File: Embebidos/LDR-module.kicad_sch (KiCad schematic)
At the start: 10 parts, among them U2 LM358

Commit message: anotaciones_fix
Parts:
- renumbered R14 to R15, R15 to R16, R16 to R17, R17 to R18
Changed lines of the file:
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@@
   (symbol (lib_id "Device:R") (at 144.78 43.18 0) (unit 1)
     (in_bom yes) (on_board yes) (fields_autoplaced)
-    (property "Reference" "R17" (id 0) (at 147.32 41.9099 0)
+    (property "Reference" "R18" (id 0) (at 147.32 41.9099 0)
       (effects (font (size 1.27 1.27)) (justify left))
     )
@@
   (symbol (lib_id "power:GND") (at 55.88 67.31 0) (unit 1)
     (in_bom yes) (on_board yes) (fields_autoplaced)
-    (property "Reference" "#PWR018" (id 0) (at 55.88 73.66 0)
+    (property "Reference" "#PWR019" (id 0) (at 55.88 73.66 0)
       (effects (font (size 1.27 1.27)) hide)
     )
@@
   (symbol (lib_id "power:GND") (at 116.84 54.61 0) (unit 1)
     (in_bom yes) (on_board yes) (fields_autoplaced)
-    (property "Reference" "#PWR021" (id 0) (at 116.84 60.96 0)
+    (property "Reference" "#PWR022" (id 0) (at 116.84 60.96 0)
       (effects (font (size 1.27 1.27)) hide)
     )
@@
   (symbol (lib_id "Device:R") (at 68.58 54.61 0) (unit 1)
     (in_bom yes) (on_board yes) (fields_autoplaced)
-    (property "Reference" "R14" (id 0) (at 71.12 53.3399 0)
+    (property "Reference" "R15" (id 0) (at 71.12 53.3399 0)
       (effects (font (size 1.27 1.27)) (justify left))
     )
@@
   (symbol (lib_id "Sensor_Optical:LDR07") (at 96.52 67.31 0) (unit 1)
     (in_bom yes) (on_board yes) (fields_autoplaced)
-    (property "Reference" "R16" (id 0) (at 99.06 66.0399 0)
+    (property "Reference" "R17" (id 0) (at 99.06 66.0399 0)
       (effects (font (size 1.27 1.27)) (justify left))
     )
@@
   (symbol (lib_id "Device:R") (at 96.52 54.61 0) (unit 1)
     (in_bom yes) (on_board yes) (fields_autoplaced)
-    (property "Reference" "R15" (id 0) (at 99.06 53.3399 0)
+    (property "Reference" "R16" (id 0) (at 99.06 53.3399 0)
       (effects (font (size 1.27 1.27)) (justify left))
     )
@@
   (symbol (lib_id "power:+5V") (at 55.88 46.99 0) (unit 1)
     (in_bom yes) (on_board yes) (fields_autoplaced)
-    (property "Reference" "#PWR017" (id 0) (at 55.88 50.8 0)
+    (property "Reference" "#PWR018" (id 0) (at 55.88 50.8 0)
       (effects (font (size 1.27 1.27)) hide)
     )
@@
   (symbol (lib_id "power:GND") (at 90.17 77.47 0) (unit 1)
     (in_bom yes) (on_board yes) (fields_autoplaced)
-    (property "Reference" "#PWR020" (id 0) (at 90.17 83.82 0)
+    (property "Reference" "#PWR021" (id 0) (at 90.17 83.82 0)
       (effects (font (size 1.27 1.27)) hide)
     )
@@
   (symbol (lib_id "power:+5V") (at 90.17 35.56 0) (unit 1)
     (in_bom yes) (on_board yes) (fields_autoplaced)
-    (property "Reference" "#PWR019" (id 0) (at 90.17 39.37 0)
-      (effects (font (size 1.27 1.27)) hide)
-    )
+    (property "Reference" "#PWR020" (id 0) (at 90.17 39.37 0)
+      (effects (font (size 1.27 1.27)) hide)
+    )

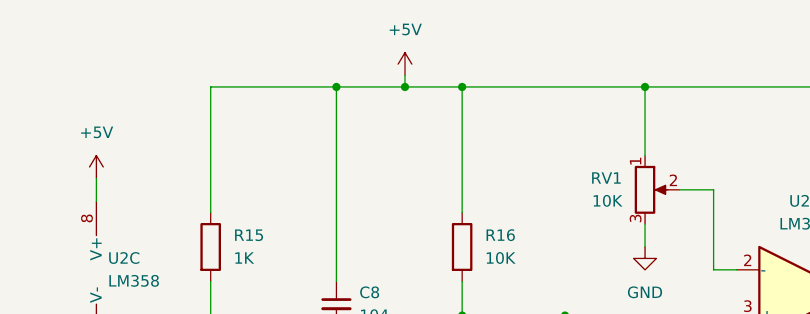
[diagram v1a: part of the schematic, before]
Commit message: cambio LDR
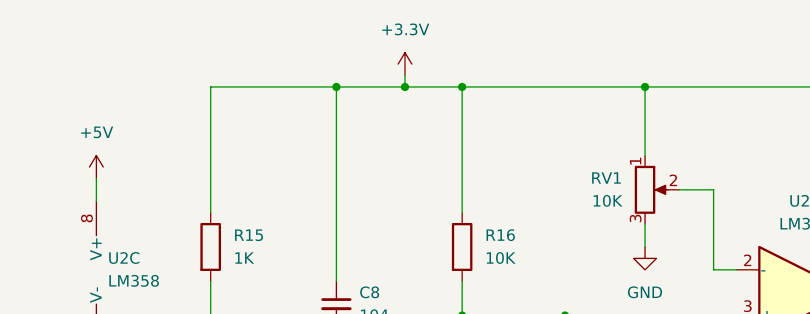
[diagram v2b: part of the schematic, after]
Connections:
- net +5V: no longer C8.1, R15.1, R16.1, R18.1, RV1.1
- new net +3.3V: C8.1, R15.1, R16.1, R18.1, RV1.1
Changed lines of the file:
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@@
     (pin "2")
+  )
+  (symbol (lib_id "power:+3.3V") (at 90.17 35.56 0) (unit 1)
+    (in_bom yes) (on_board yes) (fields_autoplaced)
+    (property "Reference" "#PWR?" (id 0) (at 90.17 39.37 0)
+      (effects (font (size 1.27 1.27)) hide)
+    )
+    (property "Value" "+3.3V" (id 1) (at 90.17 30.48 0))
+    (property "Footprint" "" (id 2) (at 90.17 35.56 0)
+      (effects (font (size 1.27 1.27)) hide)
+    )
+    (property "Datasheet" "" (id 3) (at 90.17 35.56 0)
+      (effects (font (size 1.27 1.27)) hide)
+    )
+    (pin "1")
   )
   (symbol (lib_id "power:GND") (at 55.88 67.31 0) (unit 1)
@@
       (effects (font (size 1.27 1.27)) hide)
     )
-    (pin "1")
-  )
-  (symbol (lib_id "power:+5V") (at 90.17 35.56 0) (unit 1)
-    (in_bom yes) (on_board yes) (fields_autoplaced)
-    (property "Reference" "#PWR020" (id 0) (at 90.17 39.37 0)
-      (effects (font (size 1.27 1.27)) hide)
-    )
-    (property "Value" "+5V" (id 1) (at 90.17 30.48 0))
-    (property "Footprint" "" (id 2) (at 90.17 35.56 0)
-      (effects (font (size 1.27 1.27)) hide)
-    )
-    (property "Datasheet" "" (id 3) (at 90.17 35.56 0)
-      (effects (font (size 1.27 1.27)) hide)
-    )

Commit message: wii
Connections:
- net +3.3V is gone; now on net +5V: C8.1, R15.1, R16.1, R18.1, RV1.1
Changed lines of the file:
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@@
     (pin "2")
-  )
-  (symbol (lib_id "power:+3.3V") (at 90.17 35.56 0) (unit 1)
-    (in_bom yes) (on_board yes) (fields_autoplaced)
-    (property "Reference" "#PWR?" (id 0) (at 90.17 39.37 0)
-      (effects (font (size 1.27 1.27)) hide)
-    )
-    (property "Value" "+3.3V" (id 1) (at 90.17 30.48 0))
-    (property "Footprint" "" (id 2) (at 90.17 35.56 0)
-      (effects (font (size 1.27 1.27)) hide)
-    )
-    (property "Datasheet" "" (id 3) (at 90.17 35.56 0)
-      (effects (font (size 1.27 1.27)) hide)
-    )
-    (pin "1")
   )
   (symbol (lib_id "power:GND") (at 55.88 67.31 0) (unit 1)
@@
       (effects (font (size 1.27 1.27)) hide)
     )
+    (pin "1")
+  )
+  (symbol (lib_id "power:+5V") (at 90.17 35.56 0) (unit 1)
+    (in_bom yes) (on_board yes) (fields_autoplaced)
+    (property "Reference" "#PWR020" (id 0) (at 90.17 39.37 0)
+      (effects (font (size 1.27 1.27)) hide)
+    )
+    (property "Value" "+5V" (id 1) (at 90.17 30.48 0))
+    (property "Footprint" "" (id 2) (at 90.17 35.56 0)
+      (effects (font (size 1.27 1.27)) hide)
+    )
+    (property "Datasheet" "" (id 3) (at 90.17 35.56 0)
+      (effects (font (size 1.27 1.27)) hide)
+    )

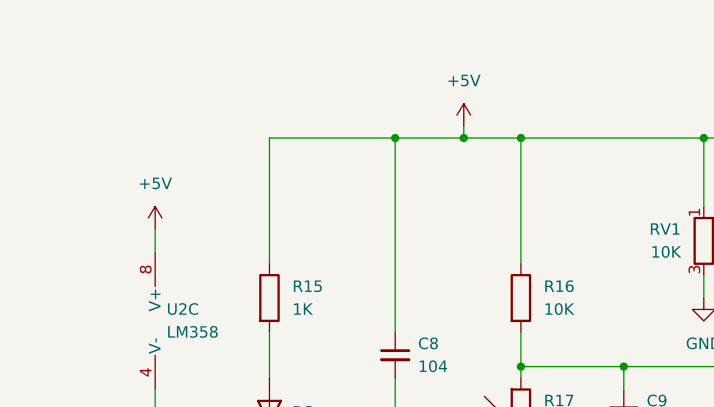
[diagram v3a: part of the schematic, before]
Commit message: Cambio de anotacion y Vcc ldr
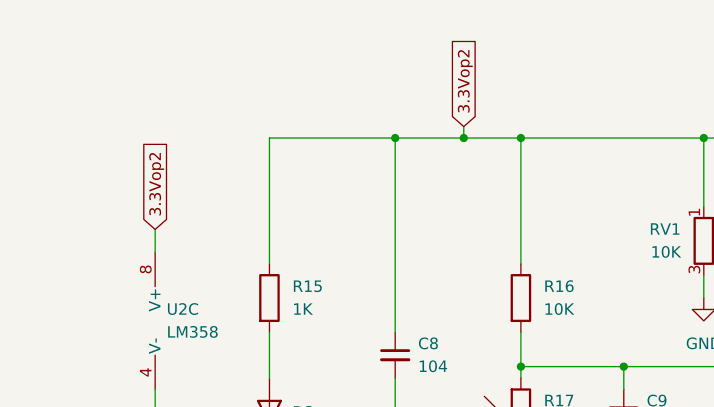
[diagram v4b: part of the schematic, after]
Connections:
- net +5V renamed 3.3Vop2
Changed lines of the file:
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@@
     (effects (font (size 1.27 1.27)) (justify left bottom))
+  )
+  (global_label "3.3Vop2" (shape input) (at 55.88 46.99 90) (fields_autoplaced)
+    (effects (font (size 1.27 1.27)) (justify left))
+    (property "Intersheet References" "${INTERSHEET_REFS}" (id 0) (at 55.8006 36.9569 90)
+      (effects (font (size 1.27 1.27)) (justify left) hide)
+    )
+  )
+  (global_label "3.3Vop2" (shape input) (at 90.17 35.56 90) (fields_autoplaced)
+    (effects (font (size 1.27 1.27)) (justify left))
+    (property "Intersheet References" "${INTERSHEET_REFS}" (id 0) (at 90.0906 25.5269 90)
+      (effects (font (size 1.27 1.27)) (justify left) hide)
+    )
   )
   (hierarchical_label "DOUT" (shape output) (at 166.37 59.69 0)
@@
   (symbol (lib_id "power:GND") (at 55.88 67.31 0) (unit 1)
     (in_bom yes) (on_board yes) (fields_autoplaced)
-    (property "Reference" "#PWR019" (id 0) (at 55.88 73.66 0)
+    (property "Reference" "#PWR021" (id 0) (at 55.88 73.66 0)
       (effects (font (size 1.27 1.27)) hide)
     )
@@
   (symbol (lib_id "power:GND") (at 116.84 54.61 0) (unit 1)
     (in_bom yes) (on_board yes) (fields_autoplaced)
-    (property "Reference" "#PWR022" (id 0) (at 116.84 60.96 0)
+    (property "Reference" "#PWR023" (id 0) (at 116.84 60.96 0)
       (effects (font (size 1.27 1.27)) hide)
     )
@@
     (pin "2")
   )
-  (symbol (lib_id "power:+5V") (at 55.88 46.99 0) (unit 1)
-    (in_bom yes) (on_board yes) (fields_autoplaced)
-    (property "Reference" "#PWR018" (id 0) (at 55.88 50.8 0)
-      (effects (font (size 1.27 1.27)) hide)
-    )
-    (property "Value" "+5V" (id 1) (at 55.88 41.91 0))
-    (property "Footprint" "" (id 2) (at 55.88 46.99 0)
-      (effects (font (size 1.27 1.27)) hide)
-    )
-    (property "Datasheet" "" (id 3) (at 55.88 46.99 0)
-      (effects (font (size 1.27 1.27)) hide)
-    )
-    (pin "1")
-  )
   (symbol (lib_id "power:GND") (at 90.17 77.47 0) (unit 1)
     (in_bom yes) (on_board yes) (fields_autoplaced)
-    (property "Reference" "#PWR021" (id 0) (at 90.17 83.82 0)
+    (property "Reference" "#PWR022" (id 0) (at 90.17 83.82 0)
       (effects (font (size 1.27 1.27)) hide)
     )
@@
       (effects (font (size 1.27 1.27)) hide)
     )
-    (pin "1")
-  )
-  (symbol (lib_id "power:+5V") (at 90.17 35.56 0) (unit 1)
-    (in_bom yes) (on_board yes) (fields_autoplaced)
-    (property "Reference" "#PWR020" (id 0) (at 90.17 39.37 0)
-      (effects (font (size 1.27 1.27)) hide)
-    )
-    (property "Value" "+5V" (id 1) (at 90.17 30.48 0))
-    (property "Footprint" "" (id 2) (at 90.17 35.56 0)
-      (effects (font (size 1.27 1.27)) hide)
-    )
-    (property "Datasheet" "" (id 3) (at 90.17 35.56 0)
-      (effects (font (size 1.27 1.27)) hide)
-    )

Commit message: Correccion errores y huellas leds LDR
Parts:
- D3, D4: footprint (none) -> LED_SMD:LED_0805_2012Metric_Pad1.15x1.40mm_HandSolder
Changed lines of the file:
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@@
       (effects (font (size 1.27 1.27)) (justify right))
     )
-    (property "Footprint" "" (id 2) (at 144.78 53.34 0)
+    (property "Footprint" "LED_SMD:LED_0805_2012Metric_Pad1.15x1.40mm_HandSolder" (id 2) (at 144.78 53.34 0)
       (effects (font (size 1.27 1.27)) hide)
     )
@@
       (effects (font (size 1.27 1.27)) (justify right))
     )
-    (property "Footprint" "" (id 2) (at 68.58 67.31 0)
+    (property "Footprint" "LED_SMD:LED_0805_2012Metric_Pad1.15x1.40mm_HandSolder" (id 2) (at 68.58 67.31 0)
       (effects (font (size 1.27 1.27)) hide)
     )

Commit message: .
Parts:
- C8, C9: footprint (none) -> Capacitor_SMD:C_0805_2012Metric_Pad1.18x1.45mm_HandSolder
- R15, R16, R18: footprint (none) -> Resistor_SMD:R_0805_2012Metric_Pad1.20x1.40mm_HandSolder
- U2: footprint (none) -> LM358DR:SOIC127P599X175-8N
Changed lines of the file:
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@@
       (effects (font (size 1.27 1.27)) (justify left))
     )
-    (property "Footprint" "" (id 2) (at 143.002 43.18 90)
+    (property "Footprint" "Resistor_SMD:R_0805_2012Metric_Pad1.20x1.40mm_HandSolder" (id 2) (at 143.002 43.18 90)
       (effects (font (size 1.27 1.27)) hide)
     )
@@
     (property "Reference" "U2" (id 0) (at 134.62 49.53 0))
     (property "Value" "LM358" (id 1) (at 134.62 52.07 0))
-    (property "Footprint" "" (id 2) (at 134.62 59.69 0)
+    (property "Footprint" "LM358DR:SOIC127P599X175-8N" (id 2) (at 134.62 59.69 0)
       (effects (font (size 1.27 1.27)) hide)
     )
@@
     (property "Reference" "U2" (id 0) (at 134.62 68.58 0))
     (property "Value" "LM358" (id 1) (at 134.62 71.12 0))
-    (property "Footprint" "" (id 2) (at 134.62 78.74 0)
+    (property "Footprint" "LM358DR:SOIC127P599X175-8N" (id 2) (at 134.62 78.74 0)
       (effects (font (size 1.27 1.27)) hide)
     )
@@
       (effects (font (size 1.27 1.27)) (justify left))
     )
-    (property "Footprint" "" (id 2) (at 66.802 54.61 90)
+    (property "Footprint" "Resistor_SMD:R_0805_2012Metric_Pad1.20x1.40mm_HandSolder" (id 2) (at 66.802 54.61 90)
       (effects (font (size 1.27 1.27)) hide)
     )
@@
       (effects (font (size 1.27 1.27)) (justify left))
     )
-    (property "Footprint" "" (id 2) (at 58.42 57.15 0)
+    (property "Footprint" "LM358DR:SOIC127P599X175-8N" (id 2) (at 58.42 57.15 0)
       (effects (font (size 1.27 1.27)) hide)
     )
@@
       (effects (font (size 1.27 1.27)) (justify left))
     )
-    (property "Footprint" "" (id 2) (at 94.742 54.61 90)
+    (property "Footprint" "Resistor_SMD:R_0805_2012Metric_Pad1.20x1.40mm_HandSolder" (id 2) (at 94.742 54.61 90)
       (effects (font (size 1.27 1.27)) hide)
     )
@@
       (effects (font (size 1.27 1.27)) (justify left))
     )
-    (property "Footprint" "" (id 2) (at 82.55 60.96 0)
+    (property "Footprint" "Capacitor_SMD:C_0805_2012Metric_Pad1.18x1.45mm_HandSolder" (id 2) (at 82.55 60.96 0)
       (effects (font (size 1.27 1.27)) hide)
     )
@@
       (effects (font (size 1.27 1.27)) (justify left))
     )
-    (property "Footprint" "" (id 2) (at 107.95 67.31 0)
-      (effects (font (size 1.27 1.27)) hide)
-    )
+    (property "Footprint" "Capacitor_SMD:C_0805_2012Metric_Pad1.18x1.45mm_HandSolder" (id 2) (at 107.95 67.31 0)
+      (effects (font (size 1.27 1.27)) hide)
+    )
